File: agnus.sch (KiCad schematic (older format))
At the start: 34 parts, among them J101 Conn_01x03_Male, J102 Jumper_2_Open, J900 Jumper_2_Bridged, U101 AGNUS8372, U102 GARY5719, U107 74F04, U108 74LS74A, U302 74LS32, U900 74F00, X1 28.63636MHz

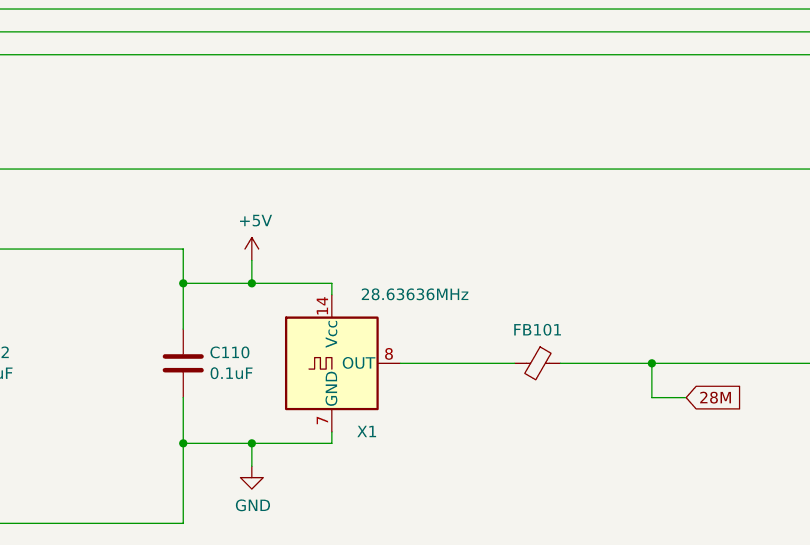
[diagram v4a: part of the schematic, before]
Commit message: Switch footprints for suitable modern replacements
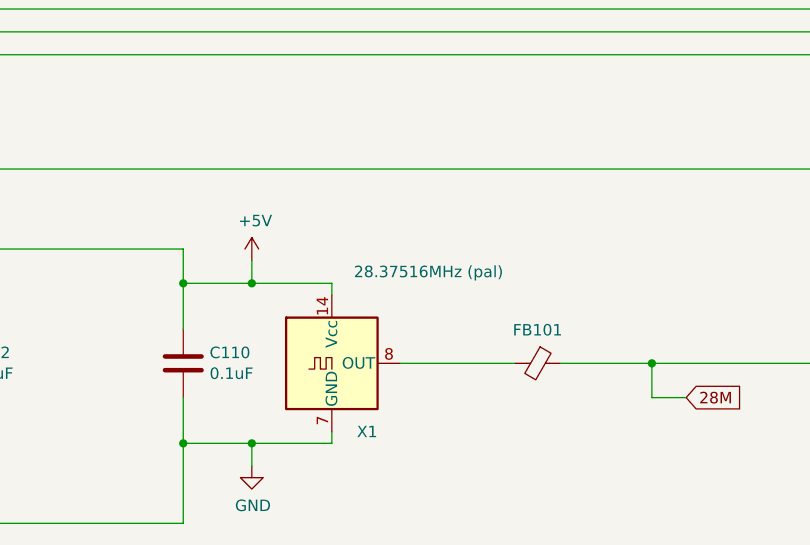
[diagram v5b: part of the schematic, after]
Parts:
- C101, C102, C107, C108, C110, C905, C907, C908, C918: footprint Capacitor_THT:C_Rect_L11.5mm_W2.0mm_P10.00mm_MKT -> Capacitor_THT:C_Rect_L11.5mm_W2.6mm_P10.00mm_MKT
- C415: footprint Capacitor_THT:CP_Radial_D8.0mm_P5.00mm -> Capacitor_THT:CP_Radial_D5.0mm_P2.50mm
- X1: value 28.63636MHz -> 28.37516MHz (pal)
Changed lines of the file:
@@
 F 0 "C905" H 1615 1096 50  0000 L CNN
 F 1 "100pF" H 1615 1005 50  0000 L CNN
-F 2 "Capacitor_THT:C_Rect_L11.5mm_W2.0mm_P10.00mm_MKT" H 1538 900 50  0001 C CNN
+F 2 "Capacitor_THT:C_Rect_L11.5mm_W2.6mm_P10.00mm_MKT" H 1538 900 50  0001 C CNN
 F 3 "~" H 1500 1050 50  0001 C CNN
 	1    1500 1050
@@
 P 4000 10500
 F 0 "X1" H 4200 10200 50  0000 R CNN
-F 1 "28.63636MHz" H 4600 10800 50  0000 R CNN
+F 1 "28.37516MHz (pal)" H 4750 10900 50  0000 R CNN
 F 2 "Oscillator:Oscillator_DIP-14" H 4450 10150 50  0001 C CNN
 F 3 "" H 3900 10500 50  0001 C CNN
@@
 F 0 "C110" H 3465 10546 50  0000 L CNN
 F 1 "0.1uF" H 3465 10455 50  0000 L CNN
-F 2 "Capacitor_THT:C_Rect_L11.5mm_W2.0mm_P10.00mm_MKT" H 3388 10350 50  0001 C CNN
+F 2 "Capacitor_THT:C_Rect_L11.5mm_W2.6mm_P10.00mm_MKT" H 3388 10350 50  0001 C CNN
 F 3 "~" H 3350 10500 50  0001 C CNN
 	1    3350 10500
@@
 F 0 "C101" H 10765 4846 50  0000 L CNN
 F 1 "0.1uF" H 10765 4755 50  0000 L CNN
-F 2 "Capacitor_THT:C_Rect_L11.5mm_W2.0mm_P10.00mm_MKT" H 10688 4650 50  0001 C CNN
+F 2 "Capacitor_THT:C_Rect_L11.5mm_W2.6mm_P10.00mm_MKT" H 10688 4650 50  0001 C CNN
 F 3 "~" H 10650 4800 50  0001 C CNN
 	1    10650 4800
@@
 F 0 "C415" H 11268 4846 50  0000 L CNN
 F 1 "4.7uF 16V" H 11268 4755 50  0000 L CNN
-F 2 "Capacitor_THT:CP_Radial_D8.0mm_P5.00mm" H 11188 4650 50  0001 C CNN
+F 2 "Capacitor_THT:CP_Radial_D5.0mm_P2.50mm" H 11188 4650 50  0001 C CNN
 F 3 "~" H 11150 4800 50  0001 C CNN
 	1    11150 4800
@@
 F 0 "C102" H 2415 10546 50  0000 L CNN
 F 1 "0.1uF" H 2415 10455 50  0000 L CNN
-F 2 "Capacitor_THT:C_Rect_L11.5mm_W2.0mm_P10.00mm_MKT" H 2338 10350 50  0001 C CNN
+F 2 "Capacitor_THT:C_Rect_L11.5mm_W2.6mm_P10.00mm_MKT" H 2338 10350 50  0001 C CNN
 F 3 "~" H 2300 10500 50  0001 C CNN
 	1    2300 10500
@@
 F 0 "C907" H 4115 4546 50  0000 L CNN
 F 1 "100pF" H 4115 4455 50  0000 L CNN
-F 2 "Capacitor_THT:C_Rect_L11.5mm_W2.0mm_P10.00mm_MKT" H 4038 4350 50  0001 C CNN
+F 2 "Capacitor_THT:C_Rect_L11.5mm_W2.6mm_P10.00mm_MKT" H 4038 4350 50  0001 C CNN
 F 3 "~" H 4000 4500 50  0001 C CNN
 	1    4000 4500
@@
 F 0 "C908" H 4615 4546 50  0000 L CNN
 F 1 "100pF" H 4615 4455 50  0000 L CNN
-F 2 "Capacitor_THT:C_Rect_L11.5mm_W2.0mm_P10.00mm_MKT" H 4538 4350 50  0001 C CNN
+F 2 "Capacitor_THT:C_Rect_L11.5mm_W2.6mm_P10.00mm_MKT" H 4538 4350 50  0001 C CNN
 F 3 "~" H 4500 4500 50  0001 C CNN
 	1    4500 4500
@@
 F 0 "C918" H 13065 7096 50  0000 L CNN
 F 1 "0.1uF" H 13065 7005 50  0000 L CNN
-F 2 "Capacitor_THT:C_Rect_L11.5mm_W2.0mm_P10.00mm_MKT" H 12988 6900 50  0001 C CNN
+F 2 "Capacitor_THT:C_Rect_L11.5mm_W2.6mm_P10.00mm_MKT" H 12988 6900 50  0001 C CNN
 F 3 "~" H 12950 7050 50  0001 C CNN
 	1    12950 7050
@@
 F 0 "C108" H 14315 7046 50  0000 L CNN
 F 1 "0.1uF" H 14315 6955 50  0000 L CNN
-F 2 "Capacitor_THT:C_Rect_L11.5mm_W2.0mm_P10.00mm_MKT" H 14238 6850 50  0001 C CNN
+F 2 "Capacitor_THT:C_Rect_L11.5mm_W2.6mm_P10.00mm_MKT" H 14238 6850 50  0001 C CNN
 F 3 "~" H 14200 7000 50  0001 C CNN
 	1    14200 7000
@@
 F 0 "C107" H 15565 7046 50  0000 L CNN
 F 1 "0.1uF" H 15565 6955 50  0000 L CNN
-F 2 "Capacitor_THT:C_Rect_L11.5mm_W2.0mm_P10.00mm_MKT" H 15488 6850 50  0001 C CNN
+F 2 "Capacitor_THT:C_Rect_L11.5mm_W2.6mm_P10.00mm_MKT" H 15488 6850 50  0001 C CNN
 F 3 "~" H 15450 7000 50  0001 C CNN
 	1    15450 7000

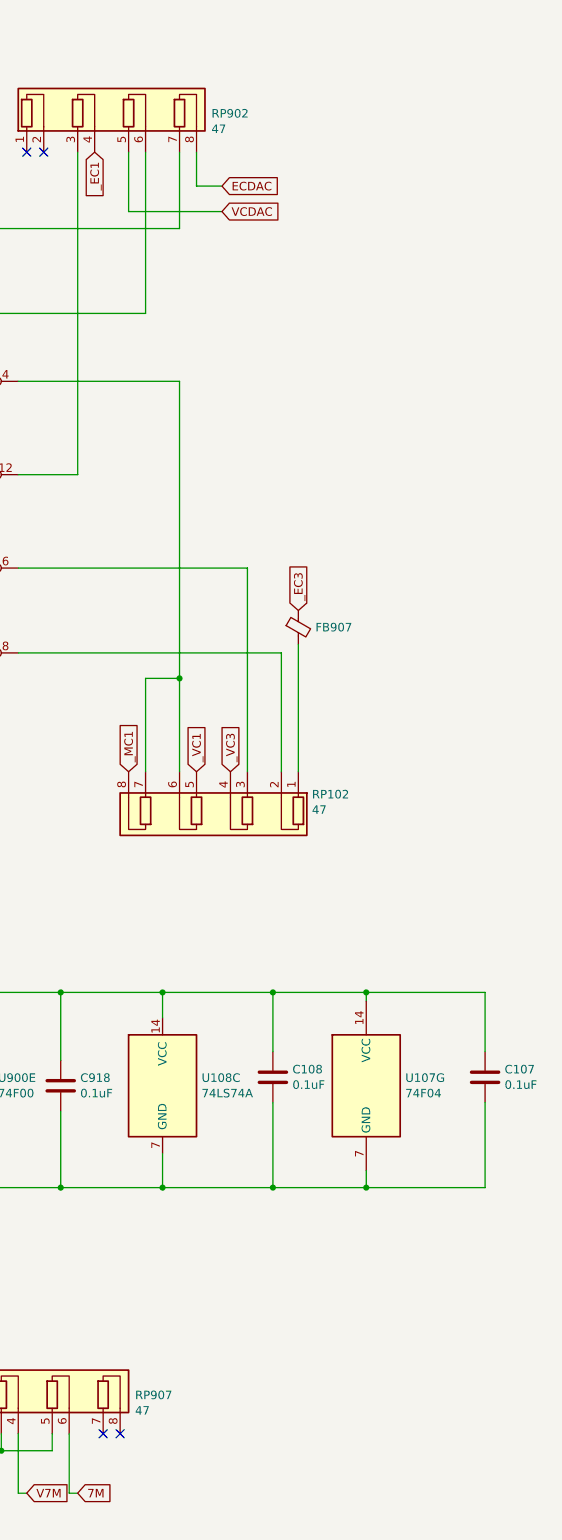
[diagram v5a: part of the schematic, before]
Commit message: Some footprints updates; Add all Mouser references
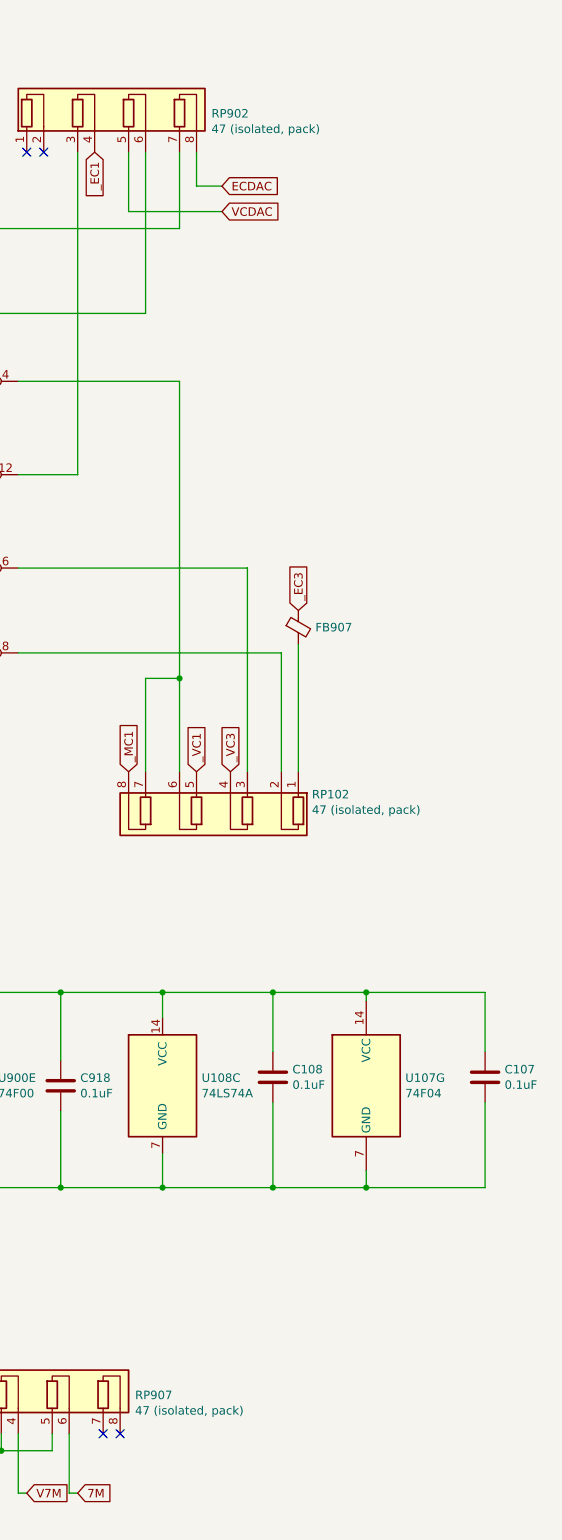
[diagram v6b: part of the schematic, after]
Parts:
- C101, C102, C107, C108, C110, C918: RefOrder (none) -> 581-SA105C104KARC
- C415: RefOrder (none) -> 647-UMA1C4R7MCD2TP
- C905, C907, C908: RefOrder (none) -> 80-C410C101K5G
- FB101, FB102, FB907: RefOrder (none) -> 875-28L0138-10R-10
- R101, R109, R916: RefOrder (none) -> 603-CFR-25JT-52-4K7
- R105, R106: RefOrder (none) -> 603-CFR-25JR-52-22R
- R110, R114, R115: RefOrder (none) -> 603-CFR-25JT-52-330R
- RP102, RP902, RP907: value 47 -> 47 (isolated, pack); RefOrder (none) -> 858-L083S470LF
- U107: RefOrder (none) -> 595-SN74F04N
- U108: RefOrder (none) -> 595-SN74LS74AN
- U302: RefOrder (none) -> 595-SN74LS32N
- U900: RefOrder (none) -> 595-SN74F00N
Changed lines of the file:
@@
 F 2 "Capacitor_THT:C_Rect_L11.5mm_W2.6mm_P10.00mm_MKT" H 1538 900 50  0001 C CNN
 F 3 "~" H 1500 1050 50  0001 C CNN
+F 4 "80-C410C101K5G" H 1500 1050 50  0001 C CNN "RefOrder"
 	1    1500 1050
 	1    0    0    -1
@@
 F 2 "Inductor_THT:L_Axial_L9.5mm_D4.0mm_P15.24mm_Horizontal_Fastron_SMCC" V 1030 1200 50  0001 C CNN
 F 3 "~" H 1100 1200 50  0001 C CNN
+F 4 "875-28L0138-10R-10" H 1100 1200 50  0001 C CNN "RefOrder"
 	1    1100 1200
 	0    1    1    0
@@
 F 2 "Resistor_THT:R_Axial_DIN0207_L6.3mm_D2.5mm_P10.16mm_Horizontal" V 1580 2200 50  0001 C CNN
 F 3 "~" H 1650 2200 50  0001 C CNN
+F 4 "603-CFR-25JR-52-22R" H 1650 2200 50  0001 C CNN "RefOrder"
 	1    1650 2200
 	0    1    1    0
@@
 F 2 "Resistor_THT:R_Axial_DIN0207_L6.3mm_D2.5mm_P10.16mm_Horizontal" V 1580 2700 50  0001 C CNN
 F 3 "~" H 1650 2700 50  0001 C CNN
+F 4 "603-CFR-25JR-52-22R" H 1650 2700 50  0001 C CNN "RefOrder"
 	1    1650 2700
 	0    1    1    0
@@
 F 2 "Resistor_THT:R_Axial_DIN0207_L6.3mm_D2.5mm_P10.16mm_Horizontal" V 1680 3350 50  0001 C CNN
 F 3 "~" H 1750 3350 50  0001 C CNN
+F 4 "603-CFR-25JT-52-4K7" H 1750 3350 50  0001 C CNN "RefOrder"
 	1    1750 3350
 	1    0    0    -1
@@
 F 2 "Resistor_THT:R_Axial_DIN0207_L6.3mm_D2.5mm_P10.16mm_Horizontal" V 5380 800 50  0001 C CNN
 F 3 "~" H 5450 800 50  0001 C CNN
+F 4 "603-CFR-25JT-52-330R" H 5450 800 50  0001 C CNN "RefOrder"
 	1    5450 800
 	1    0    0    -1
@@
 F 2 "Resistor_THT:R_Axial_DIN0207_L6.3mm_D2.5mm_P10.16mm_Horizontal" V 6030 800 50  0001 C CNN
 F 3 "~" H 6100 800 50  0001 C CNN
+F 4 "603-CFR-25JT-52-330R" H 6100 800 50  0001 C CNN "RefOrder"
 	1    6100 800
 	1    0    0    -1
@@
 F 2 "Package_DIP:DIP-14_W7.62mm_Socket" H 5050 3100 50  0001 C CNN
 F 3 "http://www.ti.com/lit/ds/symlink/sn74f00.pdf" H 5050 3100 50  0001 C CNN
+F 4 "595-SN74F00N" H 5050 3100 50  0001 C CNN "RefOrder"
 	3    5050 3100
 	-1   0    0    -1
@@
 F 2 "Package_DIP:DIP-14_W7.62mm_Socket" H 5950 3200 50  0001 C CNN
 F 3 "http://www.ti.com/lit/ds/symlink/sn74f00.pdf" H 5950 3200 50  0001 C CNN
+F 4 "595-SN74F00N" H 5950 3200 50  0001 C CNN "RefOrder"
 	4    5950 3200
 	-1   0    0    1
@@
 F 2 "Capacitor_THT:C_Rect_L11.5mm_W2.6mm_P10.00mm_MKT" H 3388 10350 50  0001 C CNN
 F 3 "~" H 3350 10500 50  0001 C CNN
+F 4 "581-SA105C104KARC" H 3350 10500 50  0001 C CNN "RefOrder"
 	1    3350 10500
 	1    0    0    -1
@@
 F 2 "Inductor_THT:L_Axial_L7.0mm_D3.3mm_P10.16mm_Horizontal_Fastron_MICC" V 4830 10500 50  0001 C CNN
 F 3 "~" H 4900 10500 50  0001 C CNN
+F 4 "875-28L0138-10R-10" H 4900 10500 50  0001 C CNN "RefOrder"
 	1    4900 10500
 	0    1    1    0
@@
 F 2 "Resistor_THT:R_Axial_DIN0207_L6.3mm_D2.5mm_P10.16mm_Horizontal" V 7780 10800 50  0001 C CNN
 F 3 "~" H 7850 10800 50  0001 C CNN
+F 4 "603-CFR-25JT-52-330R" H 7850 10800 50  0001 C CNN "RefOrder"
 	1    7850 10800
 	1    0    0    -1
@@
 F 2 "Resistor_THT:R_Axial_DIN0207_L6.3mm_D2.5mm_P10.16mm_Horizontal" V 7330 10800 50  0001 C CNN
 F 3 "~" H 7400 10800 50  0001 C CNN
+F 4 "603-CFR-25JT-52-4K7" H 7400 10800 50  0001 C CNN "RefOrder"
 	1    7400 10800
 	1    0    0    -1
@@
 F 2 "Capacitor_THT:C_Rect_L11.5mm_W2.6mm_P10.00mm_MKT" H 10688 4650 50  0001 C CNN
 F 3 "~" H 10650 4800 50  0001 C CNN
+F 4 "581-SA105C104KARC" H 10650 4800 50  0001 C CNN "RefOrder"
 	1    10650 4800
 	1    0    0    -1
@@
 F 2 "Capacitor_THT:CP_Radial_D5.0mm_P2.50mm" H 11188 4650 50  0001 C CNN
 F 3 "~" H 11150 4800 50  0001 C CNN
+F 4 "647-UMA1C4R7MCD2TP" H 11150 4800 50  0001 C CNN "RefOrder"
 	1    11150 4800
 	1    0    0    -1
@@
 F 2 "Capacitor_THT:C_Rect_L11.5mm_W2.6mm_P10.00mm_MKT" H 2338 10350 50  0001 C CNN
 F 3 "~" H 2300 10500 50  0001 C CNN
+F 4 "581-SA105C104KARC" H 2300 10500 50  0001 C CNN "RefOrder"
 	1    2300 10500
 	1    0    0    -1
@@
 F 2 "Resistor_THT:R_Axial_DIN0207_L6.3mm_D2.5mm_P10.16mm_Horizontal" V 10630 10200 50  0001 C CNN
 F 3 "~" H 10700 10200 50  0001 C CNN
+F 4 "603-CFR-25JT-52-4K7" H 10700 10200 50  0001 C CNN "RefOrder"
 	1    10700 10200
 	1    0    0    -1
@@
 F 2 "Package_DIP:DIP-14_W7.62mm_Socket" H 11700 8800 50  0001 C CNN
 F 3 "http://www.ti.com/lit/gpn/sn74LS32" H 11700 8800 50  0001 C CNN
+F 4 "595-SN74LS32N" H 11700 8800 50  0001 C CNN "RefOrder"
 	3    11700 8800
 	1    0    0    -1
@@
 P 12800 8900
 F 0 "RP907" H 13388 8927 50  0000 L CNN
-F 1 "47" H 13388 8836 50  0000 L CNN
+F 1 "47 (isolated, pack)" H 13388 8836 50  0000 L CNN
 F 2 "Resistor_THT:R_Array_SIP8" V 13475 8900 50  0001 C CNN
 F 3 "http://www.vishay.com/docs/31509/csc.pdf" H 12800 8900 50  0001 C CNN
+F 4 "858-L083S470LF" H 12800 8900 50  0001 C CNN "RefOrder"
 	1    12800 8900
 	1    0    0    -1
@@
 F 2 "Package_DIP:DIP-14_W7.62mm_Socket" H 10800 2000 50  0001 C CNN
 F 3 "https://www.soemtron.org/downloads/disposals/74f04.pdf" H 10800 2000 50  0001 C CNN
+F 4 "595-SN74F04N" H 10800 2000 50  0001 C CNN "RefOrder"
 	1    10800 2000
 	1    0    0    -1
@@
 F 2 "Package_DIP:DIP-14_W7.62mm_Socket" H 10800 2500 50  0001 C CNN
 F 3 "https://www.soemtron.org/downloads/disposals/74f04.pdf" H 10800 2500 50  0001 C CNN
+F 4 "595-SN74F04N" H 10800 2500 50  0001 C CNN "RefOrder"
 	5    10800 2500
 	1    0    0    -1
@@
 F 2 "Package_DIP:DIP-14_W7.62mm_Socket" H 12400 2900 50  0001 C CNN
 F 3 "https://www.soemtron.org/downloads/disposals/74f04.pdf" H 12400 2900 50  0001 C CNN
+F 4 "595-SN74F04N" H 12400 2900 50  0001 C CNN "RefOrder"
 	2    12400 2900
 	1    0    0    -1
@@
 F 2 "Package_DIP:DIP-14_W7.62mm_Socket" H 12400 3450 50  0001 C CNN
 F 3 "https://www.soemtron.org/downloads/disposals/74f04.pdf" H 12400 3450 50  0001 C CNN
+F 4 "595-SN74F04N" H 12400 3450 50  0001 C CNN "RefOrder"
 	6    12400 3450
 	1    0    0    -1
@@
 F 2 "Package_DIP:DIP-14_W7.62mm_Socket" H 12400 4000 50  0001 C CNN
 F 3 "https://www.soemtron.org/downloads/disposals/74f04.pdf" H 12400 4000 50  0001 C CNN
+F 4 "595-SN74F04N" H 12400 4000 50  0001 C CNN "RefOrder"
 	3    12400 4000
 	1    0    0    -1
@@
 F 2 "Package_DIP:DIP-14_W7.62mm_Socket" H 12400 4500 50  0001 C CNN
 F 3 "https://www.soemtron.org/downloads/disposals/74f04.pdf" H 12400 4500 50  0001 C CNN
+F 4 "595-SN74F04N" H 12400 4500 50  0001 C CNN "RefOrder"
 	4    12400 4500
 	1    0    0    -1
@@
 P 13250 1350
 F 0 "RP902" H 13838 1377 50  0000 L CNN
-F 1 "47" H 13838 1286 50  0000 L CNN
+F 1 "47 (isolated, pack)" H 13838 1286 50  0000 L CNN
 F 2 "Resistor_THT:R_Array_SIP8" V 13925 1350 50  0001 C CNN
 F 3 "http://www.vishay.com/docs/31509/csc.pdf" H 13250 1350 50  0001 C CNN
+F 4 "858-L083S470LF" H 13250 1350 50  0001 C CNN "RefOrder"
 	1    13250 1350
 	1    0    0    -1
@@
 P 13850 5400
 F 0 "RP102" H 13270 5334 50  0000 R CNN
-F 1 "47" H 13270 5425 50  0000 R CNN
+F 1 "47 (isolated, pack)" H 13270 5425 50  0000 R CNN
 F 2 "Resistor_THT:R_Array_SIP8" V 14525 5400 50  0001 C CNN
 F 3 "http://www.vishay.com/docs/31509/csc.pdf" H 13850 5400 50  0001 C CNN
+F 4 "858-L083S470LF" H 13850 5400 50  0001 C CNN "RefOrder"
 	1    13850 5400
 	-1   0    0    1
@@
 F 2 "Inductor_THT:L_Axial_L7.0mm_D3.3mm_P10.16mm_Horizontal_Fastron_MICC" V 14280 4350 50  0001 C CNN
 F 3 "~" H 14350 4350 50  0001 C CNN
+F 4 "875-28L0138-10R-10" H 14350 4350 50  0001 C CNN "RefOrder"
 	1    14350 4350
 	1    0    0    -1
@@
 F 2 "Capacitor_THT:C_Rect_L11.5mm_W2.6mm_P10.00mm_MKT" H 4038 4350 50  0001 C CNN
 F 3 "~" H 4000 4500 50  0001 C CNN
+F 4 "80-C410C101K5G" H 4000 4500 50  0001 C CNN "RefOrder"
 	1    4000 4500
 	1    0    0    -1
@@
 F 2 "Capacitor_THT:C_Rect_L11.5mm_W2.6mm_P10.00mm_MKT" H 4538 4350 50  0001 C CNN
 F 3 "~" H 4500 4500 50  0001 C CNN
+F 4 "80-C410C101K5G" H 4500 4500 50  0001 C CNN "RefOrder"
 	1    4500 4500
 	1    0    0    -1
@@
 F 2 "Package_DIP:DIP-14_W7.62mm_Socket" H 12350 7050 50  0001 C CNN
 F 3 "http://www.ti.com/lit/ds/symlink/sn74f00.pdf" H 12350 7050 50  0001 C CNN
+F 4 "595-SN74F00N" H 12350 7050 50  0001 C CNN "RefOrder"
 	5    12350 7050
 	-1   0    0    -1
@@
 F 2 "Package_DIP:DIP-14_W7.62mm_Socket" H 13550 7050 50  0001 C CNN
 F 3 "http://www.ti.com/lit/ds/symlink/sn74ls74a.pdf" H 13550 7050 50  0001 C CNN
+F 4 "595-SN74LS74AN" H 13550 7050 50  0001 C CNN "RefOrder"
 	3    13550 7050
 	1    0    0    -1
@@
 F 2 "Capacitor_THT:C_Rect_L11.5mm_W2.6mm_P10.00mm_MKT" H 12988 6900 50  0001 C CNN
 F 3 "~" H 12950 7050 50  0001 C CNN
+F 4 "581-SA105C104KARC" H 12950 7050 50  0001 C CNN "RefOrder"
 	1    12950 7050
 	1    0    0    -1
@@
 F 2 "Capacitor_THT:C_Rect_L11.5mm_W2.6mm_P10.00mm_MKT" H 14238 6850 50  0001 C CNN
 F 3 "~" H 14200 7000 50  0001 C CNN
+F 4 "581-SA105C104KARC" H 14200 7000 50  0001 C CNN "RefOrder"
 	1    14200 7000
 	1    0    0    -1
@@
 F 2 "Package_DIP:DIP-14_W7.62mm_Socket" H 14750 7050 50  0001 C CNN
 F 3 "https://www.soemtron.org/downloads/disposals/74f04.pdf" H 14750 7050 50  0001 C CNN
+F 4 "595-SN74F04N" H 14750 7050 50  0001 C CNN "RefOrder"
 	7    14750 7050
 	1    0    0    -1
@@
 F 2 "Capacitor_THT:C_Rect_L11.5mm_W2.6mm_P10.00mm_MKT" H 15488 6850 50  0001 C CNN
 F 3 "~" H 15450 7000 50  0001 C CNN
+F 4 "581-SA105C104KARC" H 15450 7000 50  0001 C CNN "RefOrder"
 	1    15450 7000
 	1    0    0    -1
